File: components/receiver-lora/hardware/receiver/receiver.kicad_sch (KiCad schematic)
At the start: 4 parts, among them J1 Conn_Coaxial_Small, U1 GY-NEO6MV2, U2 ESP32-S3-DEVKITC-1-N8R8, U3 RFM95W-915S2

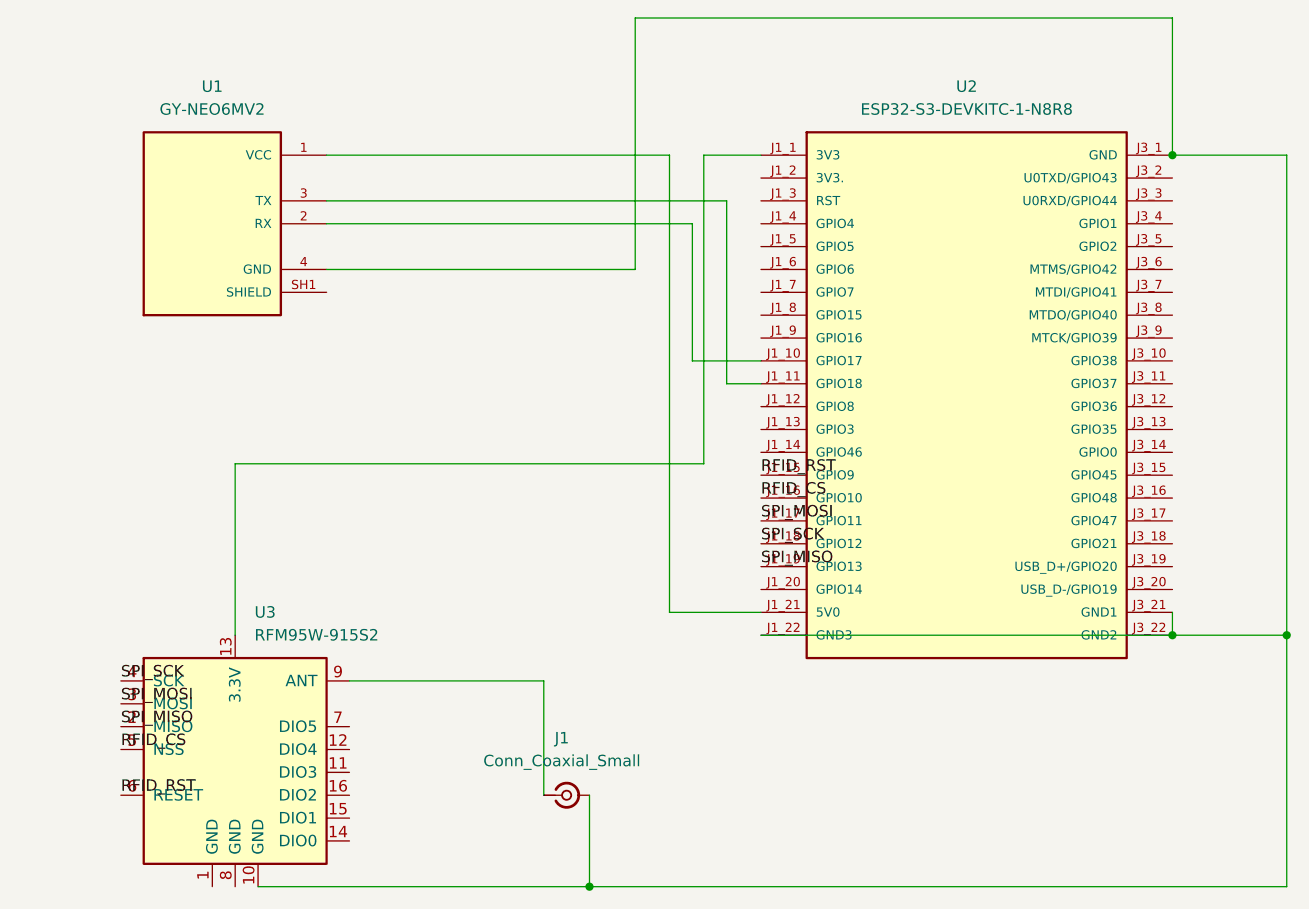
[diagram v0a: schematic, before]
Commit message: Update on receiver PCB (still need modifications)
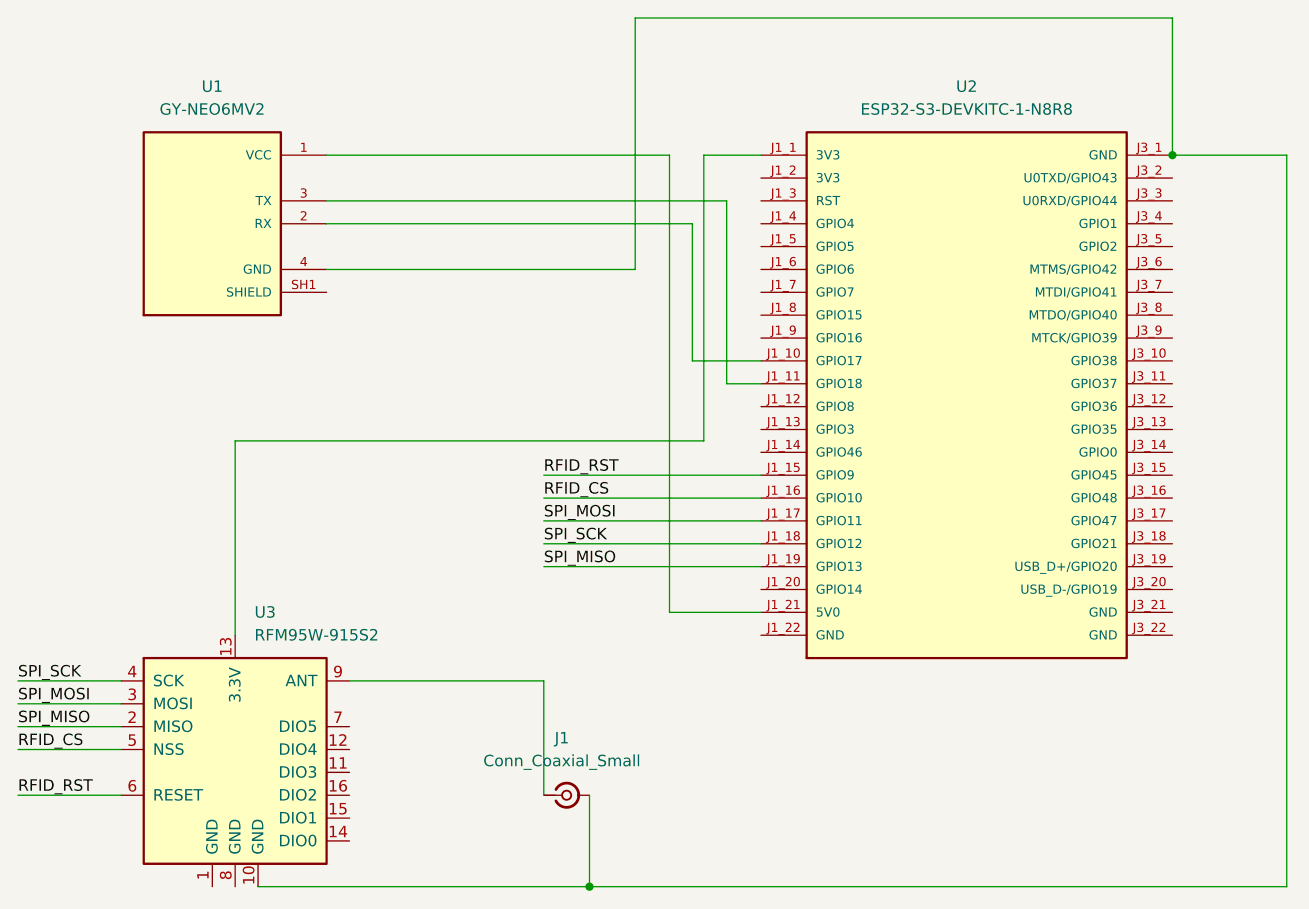
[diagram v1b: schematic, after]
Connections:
- net at J1.2 (Ext), U1.4 (GND), U2.J3_1 (GND)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: no longer U2.J1_22 (GND3), U2.J3_21 (GND1), U2.J3_22 (GND2)
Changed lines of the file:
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@@
 		(color 0 0 0 0)
 	)
-	(junction
-		(at 198.12 97.79)
-		(diameter 0)
-		(color 0 0 0 0)
-	)
-	(junction
-		(at 210.82 97.79)
-		(diameter 0)
-		(color 0 0 0 0)
-	)
 	(wire
 		(pts
@@
 	(wire
 		(pts
+			(xy 69.85 107.95) (xy 81.28 107.95)
+		)
+		(stroke
+			(width 0)
+			(type default)
+		)
+	)
+	(wire
+		(pts
 			(xy 198.12 29.21) (xy 198.12 44.45)
 		)
@@
 	(wire
 		(pts
+			(xy 128.27 87.63) (xy 152.4 87.63)
+		)
+		(stroke
+			(width 0)
+			(type default)
+		)
+	)
+	(wire
+		(pts
 			(xy 104.14 49.53) (xy 148.59 49.53)
 		)
@@
 	(wire
 		(pts
-			(xy 152.4 97.79) (xy 198.12 97.79)
-		)
-		(stroke
-			(width 0)
-			(type default)
-		)
-	)
-	(wire
-		(pts
 			(xy 96.52 125.73) (xy 133.35 125.73)
 		)
@@
 	(wire
 		(pts
+			(xy 69.85 115.57) (xy 81.28 115.57)
+		)
+		(stroke
+			(width 0)
+			(type default)
+		)
+	)
+	(wire
+		(pts
 			(xy 144.78 52.07) (xy 144.78 67.31)
 		)
@@
 	(wire
 		(pts
-			(xy 198.12 95.25) (xy 198.12 97.79)
-		)
-		(stroke
-			(width 0)
-			(type default)
-		)
-	)
-	(wire
-		(pts
 			(xy 104.14 44.45) (xy 142.24 44.45)
 		)
@@
 	(wire
 		(pts
-			(xy 146.05 78.74) (xy 146.05 44.45)
+			(xy 128.27 90.17) (xy 152.4 90.17)
+		)
+		(stroke
+			(width 0)
+			(type default)
+		)
+	)
+	(wire
+		(pts
+			(xy 128.27 82.55) (xy 152.4 82.55)
+		)
+		(stroke
+			(width 0)
+			(type default)
+		)
+	)
+	(wire
+		(pts
+			(xy 146.05 76.2) (xy 146.05 44.45)
 		)
 		(stroke
@@
 	(wire
 		(pts
-			(xy 210.82 97.79) (xy 210.82 125.73)
+			(xy 69.85 102.87) (xy 81.28 102.87)
+		)
+		(stroke
+			(width 0)
+			(type default)
+		)
+	)
+	(wire
+		(pts
+			(xy 69.85 105.41) (xy 81.28 105.41)
 		)
 		(stroke
@@
 	(wire
 		(pts
+			(xy 128.27 85.09) (xy 152.4 85.09)
+		)
+		(stroke
+			(width 0)
+			(type default)
+		)
+	)
+	(wire
+		(pts
+			(xy 128.27 80.01) (xy 152.4 80.01)
+		)
+		(stroke
+			(width 0)
+			(type default)
+		)
+	)
+	(wire
+		(pts
 			(xy 104.14 57.15) (xy 138.43 57.15)
 		)
@@
 	(wire
 		(pts
-			(xy 198.12 97.79) (xy 210.82 97.79)
-		)
-		(stroke
-			(width 0)
-			(type default)
-		)
-	)
-	(wire
-		(pts
 			(xy 198.12 44.45) (xy 210.82 44.45)
 		)
@@
 	(wire
 		(pts
-			(xy 210.82 44.45) (xy 210.82 97.79)
+			(xy 210.82 44.45) (xy 210.82 125.73)
 		)
 		(stroke
@@
 	(wire
 		(pts
-			(xy 93.98 78.74) (xy 146.05 78.74)
+			(xy 93.98 76.2) (xy 146.05 76.2)
 		)
 		(stroke
@@
 	(wire
 		(pts
-			(xy 93.98 97.79) (xy 93.98 78.74)
+			(xy 93.98 97.79) (xy 93.98 76.2)
 		)
 		(stroke
@@
 		)
 	)
+	(wire
+		(pts
+			(xy 69.85 110.49) (xy 81.28 110.49)
+		)
+		(stroke
+			(width 0)
+			(type default)
+		)
+	)
 	(label "SPI_SCK"
-		(at 152.4 87.63 0)
+		(at 128.27 87.63 0)
 		(effects
 			(font
@@
 	)
 	(label "SPI_MOSI"
-		(at 152.4 85.09 0)
+		(at 128.27 85.09 0)
 		(effects
 			(font
@@
 	)
 	(label "RFID_RST"
-		(at 81.28 115.57 0)
+		(at 69.85 115.57 0)
 		(effects
 			(font
@@
 	)
 	(label "SPI_MISO"
-		(at 152.4 90.17 0)
+		(at 128.27 90.17 0)
 		(effects
 			(font
@@
 	)
 	(label "SPI_MISO"
-		(at 81.28 107.95 0)
+		(at 69.85 107.95 0)
 		(effects
 			(font
@@
 	)
 	(label "RFID_CS"
-		(at 152.4 82.55 0)
+		(at 128.27 82.55 0)
 		(effects
 			(font
@@
 	)
 	(label "RFID_RST"
-		(at 152.4 80.01 0)
+		(at 128.27 80.01 0)
 		(effects
 			(font
@@
 	)
 	(label "SPI_SCK"
-		(at 81.28 102.87 0)
+		(at 69.85 102.87 0)
 		(effects
 			(font
@@
 	)
 	(label "RFID_CS"
-		(at 81.28 110.49 0)
+		(at 69.85 110.49 0)
 		(effects
 			(font
@@
 	)
 	(label "SPI_MOSI"
-		(at 81.28 105.41 0)
-		(effects
-			(font
+		(at 69.85 105.41 0)
+		(effects
+			(font
